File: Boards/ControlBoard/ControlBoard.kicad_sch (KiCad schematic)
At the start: 12 parts, among them J1 TBP02R2W-381-06BE, J11 Conn_02x10_Counter_Clockwise, J12 Conn_02x10_Counter_Clockwise, J13 Conn_02x10_Counter_Clockwise, J14 Conn_02x10_Counter_Clockwise, J2 TBP02R2W-381-06BE, J23 776231-1, J3 TBP01R2W-508-02BE, J4 TBP01R1-508-04BE, J5 Conn_02x10_Counter_Clockwise, J7 TBP02R2W-381-08BE, J8 TBP02R2W-381-08BE

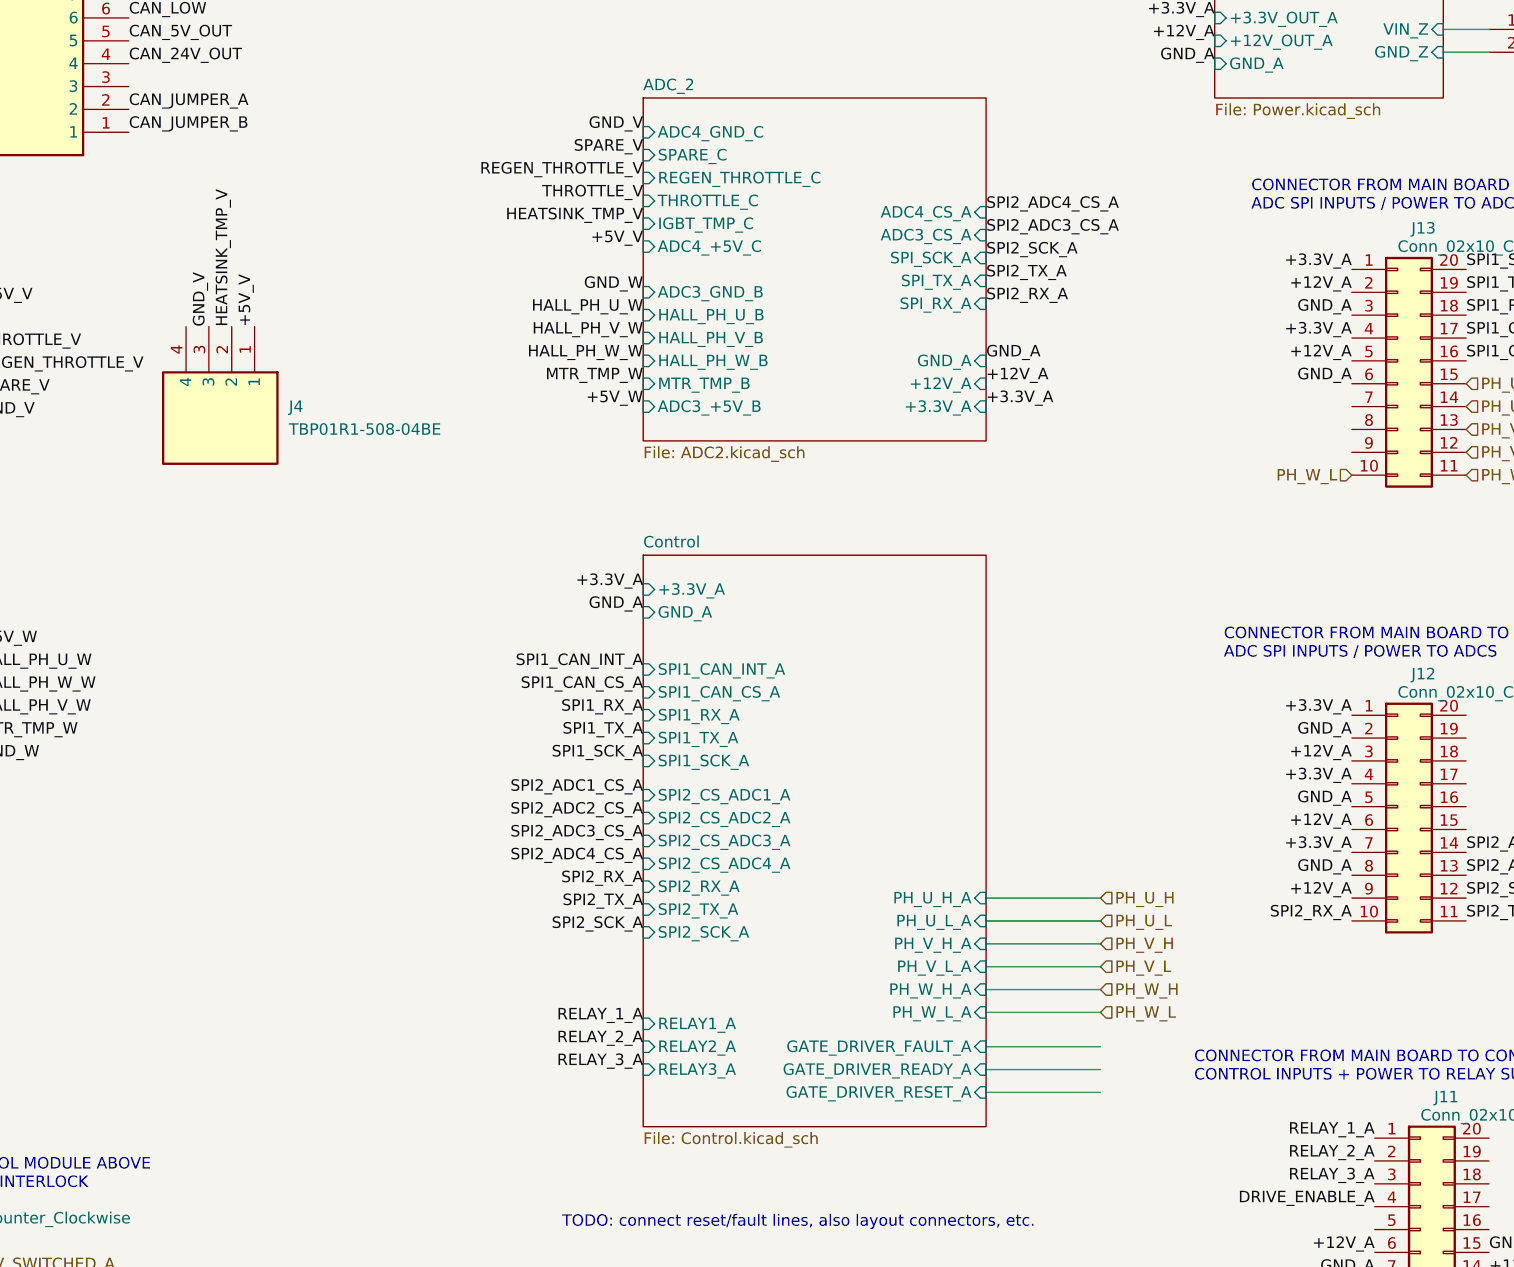
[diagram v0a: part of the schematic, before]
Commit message: layout control boards, add baseplate, refine mechanical layout
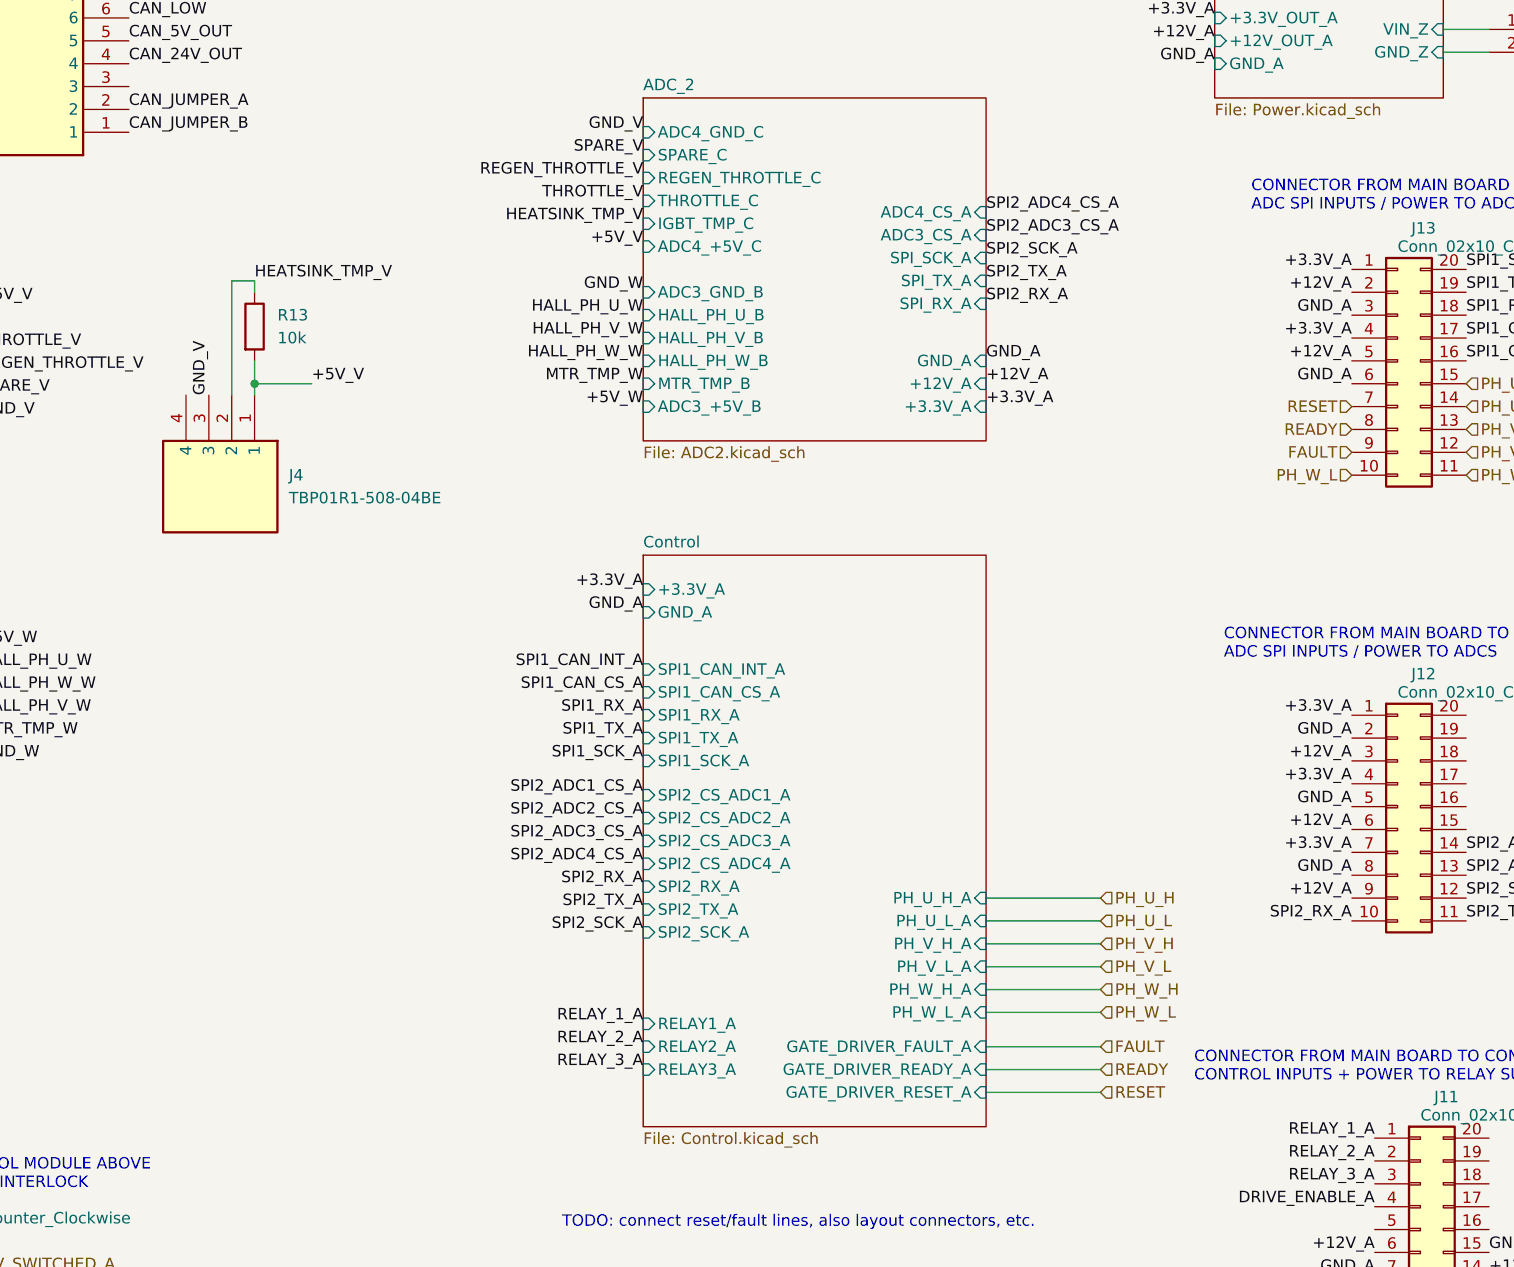
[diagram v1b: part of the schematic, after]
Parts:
- added R13: 10k, Resistor_SMD:R_1210_3225Metric_Pad1.30x2.65mm_HandSolder, symbol Device:R
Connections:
- net +5V_V: now also R13.2
- net HEATSINK_TMP_V: now also R13.1
- net RESET: now reaches J13.7 (Pin_7)
- net READY: now reaches J13.8 (Pin_8)
- net FAULT: now reaches J13.9 (Pin_9)
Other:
- moved on the sheet: J4
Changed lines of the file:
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@@
 		)
+	)
+	(junction
+		(at 71.12 69.85)
+		(diameter 0)
+		(color 0 0 0 0)
 	)
 	(wire
@@
 	(wire
 		(pts
-			(xy 152.4 134.62) (xy 165.1 134.62)
+			(xy 71.12 58.42) (xy 68.58 58.42)
 		)
 		(stroke
@@
 	(wire
 		(pts
-			(xy 203.2 33.02) (xy 208.28 33.02)
+			(xy 152.4 134.62) (xy 165.1 134.62)
 		)
 		(stroke
@@
 	(wire
 		(pts
-			(xy 152.4 137.16) (xy 165.1 137.16)
+			(xy 203.2 33.02) (xy 208.28 33.02)
 		)
 		(stroke
@@
 	(wire
 		(pts
-			(xy 152.4 139.7) (xy 165.1 139.7)
+			(xy 152.4 137.16) (xy 165.1 137.16)
 		)
 		(stroke
@@
 	(wire
 		(pts
-			(xy 152.4 146.05) (xy 165.1 146.05)
+			(xy 152.4 139.7) (xy 165.1 139.7)
 		)
 		(stroke
@@
 	(wire
 		(pts
-			(xy 152.4 132.08) (xy 165.1 132.08)
+			(xy 152.4 146.05) (xy 165.1 146.05)
 		)
 		(stroke
@@
 	(wire
 		(pts
-			(xy 203.2 30.48) (xy 208.28 30.48)
+			(xy 152.4 132.08) (xy 165.1 132.08)
 		)
 		(stroke
@@
 	(wire
 		(pts
-			(xy 152.4 127) (xy 165.1 127)
+			(xy 203.2 30.48) (xy 208.28 30.48)
 		)
 		(stroke
@@
 	(wire
 		(pts
-			(xy 152.4 129.54) (xy 165.1 129.54)
+			(xy 68.58 58.42) (xy 68.58 71.12)
 		)
 		(stroke
@@
 	(wire
 		(pts
-			(xy 152.4 143.51) (xy 165.1 143.51)
+			(xy 152.4 127) (xy 165.1 127)
 		)
 		(stroke
@@
 		)
 	)
+	(wire
+		(pts
+			(xy 152.4 129.54) (xy 165.1 129.54)
+		)
+		(stroke
+			(width 0)
+			(type default)
+		)
+	)
+	(wire
+		(pts
+			(xy 71.12 69.85) (xy 77.47 69.85)
+		)
+		(stroke
+			(width 0)
+			(type default)
+		)
+	)
+	(wire
+		(pts
+			(xy 71.12 69.85) (xy 71.12 71.12)
+		)
+		(stroke
+			(width 0)
+			(type default)
+		)
+	)
+	(wire
+		(pts
+			(xy 152.4 143.51) (xy 165.1 143.51)
+		)
+		(stroke
+			(width 0)
+			(type default)
+		)
+	)
+	(wire
+		(pts
+			(xy 71.12 59.69) (xy 71.12 58.42)
+		)
+		(stroke
+			(width 0)
+			(type default)
+		)
+	)
+	(wire
+		(pts
+			(xy 71.12 67.31) (xy 71.12 69.85)
+		)
+		(stroke
+			(width 0)
+			(type default)
+		)
+	)
 	(label "RELAY1_COM"
 		(at 36.83 185.42 0)
@@
 	)
 	(label "+5V_V"
-		(at 71.12 63.5 90)
+		(at 77.47 69.85 0)
 		(effects
 			(font
@@
 	)
 	(label "GND_V"
-		(at 66.04 63.5 90)
+		(at 66.04 71.12 90)
 		(effects
 			(font
@@
 	)
 	(label "HEATSINK_TMP_V"
-		(at 68.58 63.5 90)
+		(at 71.12 58.42 0)
 		(effects
 			(font
@@
 			)
 			(justify right bottom)
+		)
+	)
+	(hierarchical_label "RESET"
+		(shape input)
+		(at 193.04 72.39 180)
+		(effects
+			(font
+				(size 1.27 1.27)
+			)
+			(justify right)
 		)
 	)
@@
 		)
 	)
+	(hierarchical_label "FAULT"
+		(shape input)
+		(at 193.04 77.47 180)
+		(effects
+			(font
+				(size 1.27 1.27)
+			)
+			(justify right)
+		)
+	)
 	(hierarchical_label "+12V_SWITCHED_A"
 		(shape input)
@@
 		)
 	)
+	(hierarchical_label "RESET"
+		(shape input)
+		(at 165.1 148.59 0)
+		(effects
+			(font
+				(size 1.27 1.27)
+			)
+			(justify left)
+		)
+	)
+	(hierarchical_label "FAULT"
+		(shape input)
+		(at 165.1 143.51 0)
+		(effects
+			(font
+				(size 1.27 1.27)
+			)
+			(justify left)
+		)
+	)
 	(hierarchical_label "PH_V_H"
 		(shape input)
@@
 		(shape input)
 		(at 165.1 127 0)
+		(effects
+			(font
+				(size 1.27 1.27)
+			)
+			(justify left)
+		)
+	)
+	(hierarchical_label "READY"
+		(shape input)
+		(at 193.04 74.93 180)
+		(effects
+			(font
+				(size 1.27 1.27)
+			)
+			(justify right)
+		)
+	)
+	(hierarchical_label "READY"
+		(shape input)
+		(at 165.1 146.05 0)
 		(effects
 			(font
@@
 	)
 	(symbol
+		(lib_id "Device:R")
+		(at 71.12 63.5 0)
+		(unit 1)
+		(exclude_from_sim no)
+		(in_bom yes)
+		(on_board yes)
+		(dnp no)
+		(fields_autoplaced yes)
+		(property "Reference" "R13"
+			(at 73.66 62.2299 0)
+			(effects
+				(font
+					(size 1.27 1.27)
+				)
+				(justify left)
+			)
+		)
+		(property "Value" "10k"
+			(at 73.66 64.7699 0)
+			(effects
+				(font
+					(size 1.27 1.27)
+				)
+				(justify left)
+			)
+		)
+		(property "Footprint" "Resistor_SMD:R_1210_3225Metric_Pad1.30x2.65mm_HandSolder"
+			(at 69.342 63.5 90)
+			(effects
+				(font
+					(size 1.27 1.27)
+				)
+				(hide yes)
+			)
+		)
+		(property "Datasheet" "~"
+			(at 71.12 63.5 0)
+			(effects
+				(font
+					(size 1.27 1.27)
+				)
+				(hide yes)
+			)
+		)
+		(property "Description" "Resistor"
+			(at 71.12 63.5 0)
+			(effects
+				(font
+					(size 1.27 1.27)
+				)
+				(hide yes)
+			)
+		)
+		(pin "1"
+		)
+		(pin "2"
+		)
+		(instances
+			(project "ControlBoard"
+				(path "/66e49eb5-2741-49e2-b48a-baf482488ca8"
+					(reference "R13")
+					(unit 1)
+				)
+			)
+		)
+	)
+	(symbol
 		(lib_id "InverterCom:TBP01R2W-508-02BE")
 		(at 208.28 30.48 0)
@@
 	(symbol
 		(lib_id "InverterCom:TBP01R1-508-04BE")
-		(at 71.12 63.5 270)
+		(at 71.12 71.12 270)
 		(unit 1)
 		(exclude_from_sim no)
@@
 		(fields_autoplaced yes)
 		(property "Reference" "J4"
-			(at 74.93 72.3899 90)
+			(at 74.93 80.0099 90)
 			(effects
 				(font
@@
 		)
 		(property "Value" "TBP01R1-508-04BE"
-			(at 74.93 74.9299 90)
+			(at 74.93 82.5499 90)
 			(effects
 				(font
@@
 		)
 		(property "Footprint" "TBP01R150804BE"
-			(at -23.8 80.01 0)
+			(at -23.8 87.63 0)
 			(effects
 				(font
@@
 		)
 		(property "Datasheet" "https://www.sameskydevices.com/product/resource/supplyframepdf/tbp01r1-508.pdf"
-			(at -123.8 80.01 0)
+			(at -123.8 87.63 0)
 			(effects
 				(font
@@
 		)
 		(property "Description" "2~24 Poles, Pluggable, Receptacle, Horizontal, 5.08 Pitch, Terminal Block Connector"
-			(at 71.12 63.5 0)
+			(at 71.12 71.12 0)
 			(effects
 				(font
@@
 		)
 		(property "Height" "8.9"
-			(at -323.8 80.01 0)
+			(at -323.8 87.63 0)
 			(effects
 				(font
@@
 		)
 		(property "Mouser Part Number" "490-TBP01R1-508-04BE"
-			(at -423.8 80.01 0)
+			(at -423.8 87.63 0)
 			(effects
 				(font
@@
 		)
 		(property "Mouser Price/Stock" "https://www.mouser.co.uk/ProductDetail/Same-Sky/TBP01R1-508-04BE?qs=PzGy0jfpSMtbuigPwCNi2Q%3D%3D"
-			(at -523.8 80.01 0)
+			(at -523.8 87.63 0)
 			(effects
 				(font
@@
 		)
 		(property "Manufacturer_Name" "Same Sky"
-			(at -623.8 80.01 0)
+			(at -623.8 87.63 0)
 			(effects
 				(font
@@
 		)
 		(property "Manufacturer_Part_Number" "TBP01R1-508-04BE"
-			(at -723.8 80.01 0)
-			(effects
-				(font
+			(at -723.8 87.63 0)
+			(effects
+				(font

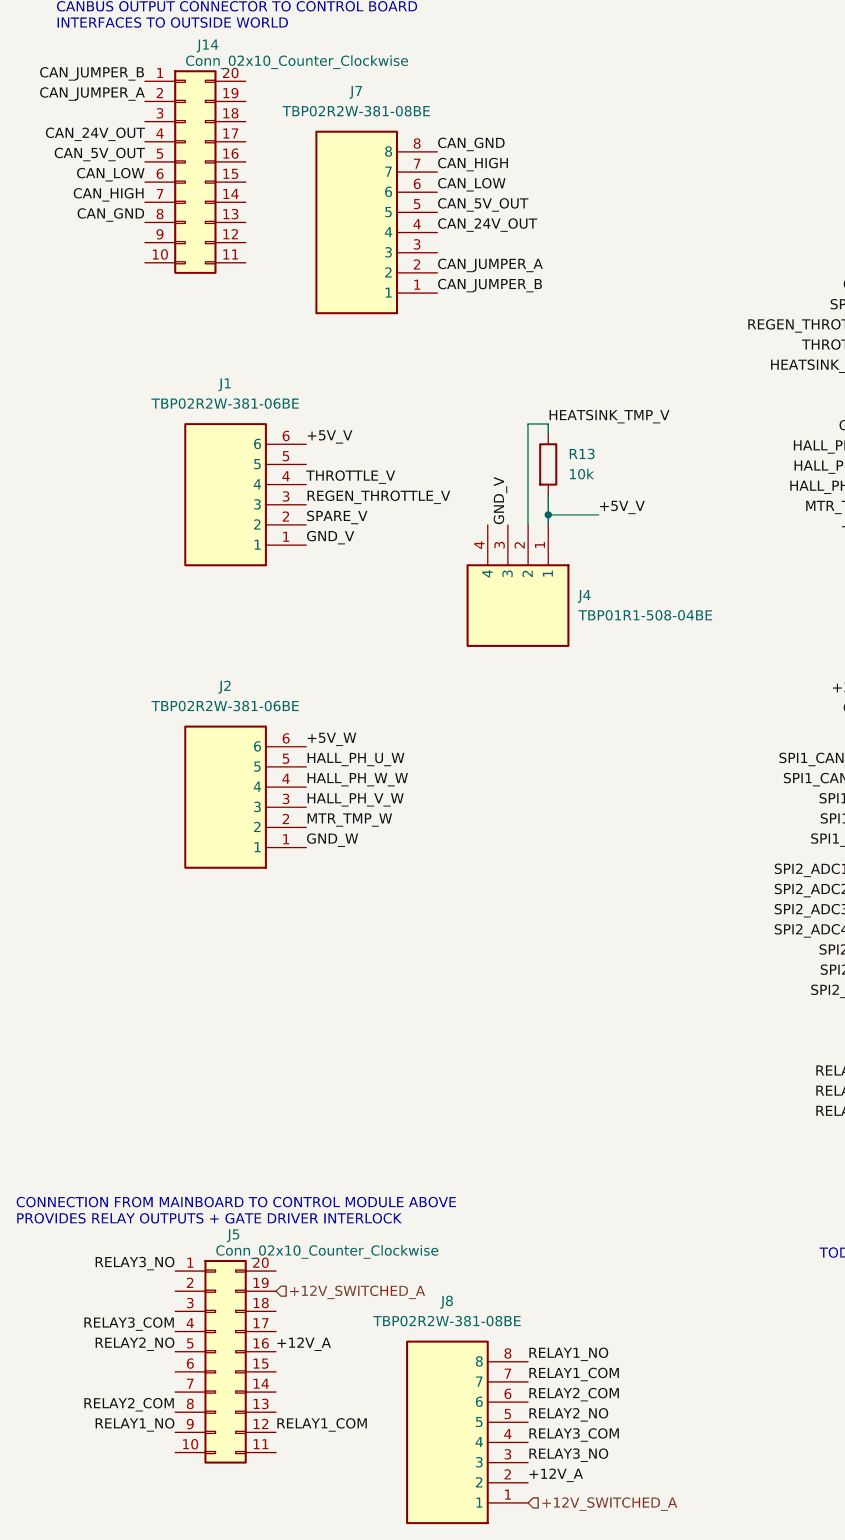
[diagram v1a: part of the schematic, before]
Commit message: Layout mainboard, add EMI filter caps
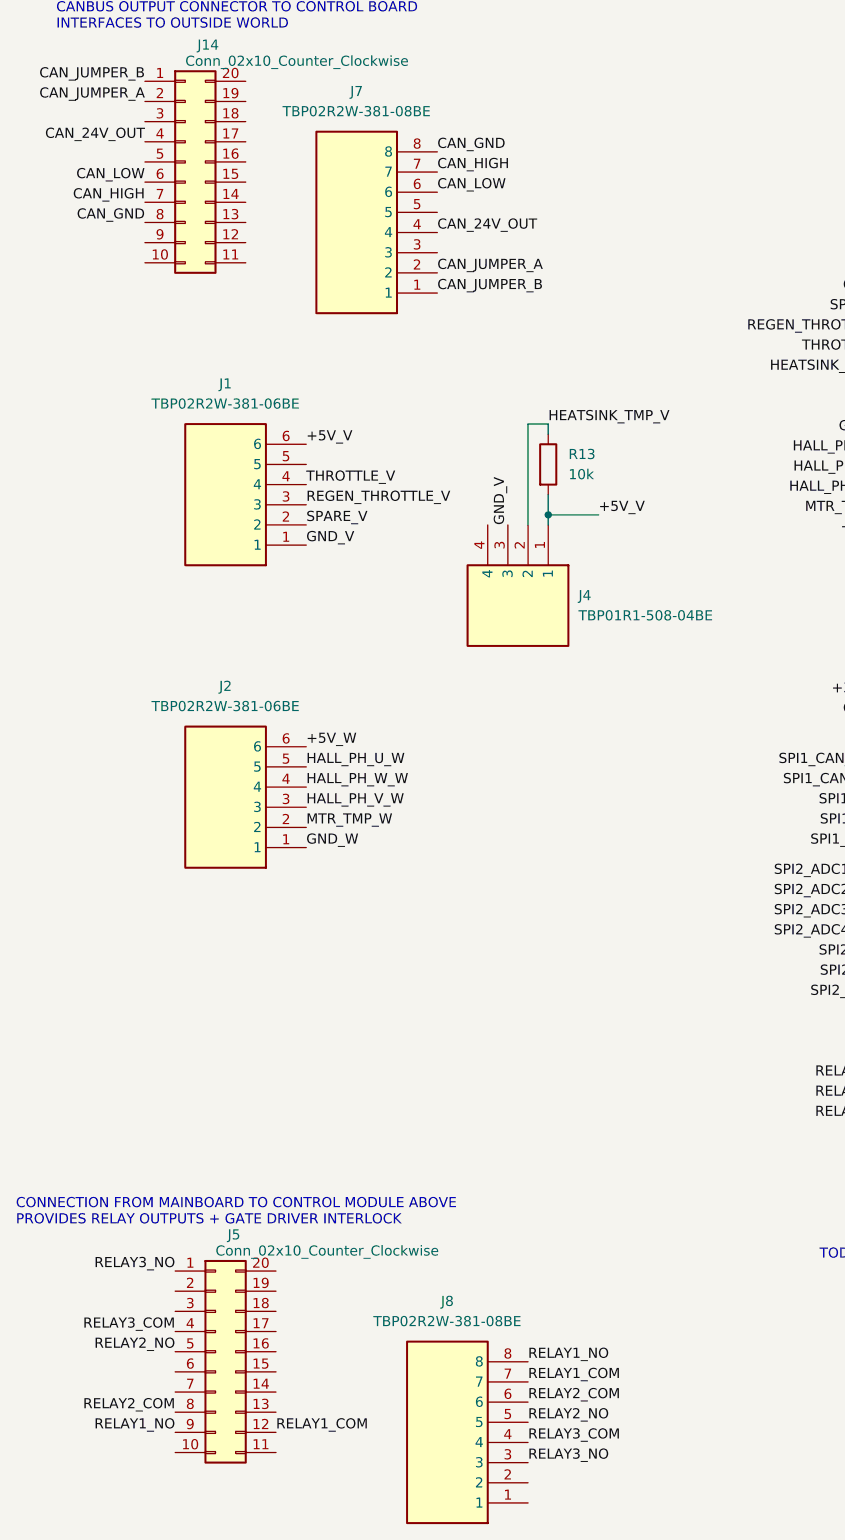
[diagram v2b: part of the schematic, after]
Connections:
- net +12V_A: no longer J5.16 (Pin_16), J8.2
- net +12V_SWITCHED_A: no longer names the net of J8.1
- net +12V_SWITCHED_A: no longer J5.19 (Pin_19)
- net CAN_5V_OUT: no longer names the net of J14.5 (Pin_5)
- net CAN_5V_OUT: no longer J7.5
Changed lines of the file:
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@@
-		)
-	)
-	(label "CAN_5V_OUT"
-		(at 57.15 31.75 0)
-		(effects
-			(font
-				(size 1.27 1.27)
-			)
-			(justify left bottom)
 		)
 	)
@@
 		)
 	)
-	(label "+12V_A"
-		(at 36.83 175.26 0)
-		(effects
-			(font
-				(size 1.27 1.27)
-			)
-			(justify left bottom)
-		)
-	)
-	(label "CAN_5V_OUT"
-		(at 20.32 25.4 180)
-		(effects
-			(font
-				(size 1.27 1.27)
-			)
-			(justify right bottom)
-		)
-	)
 	(label "GND_V"
 		(at 40.64 73.66 0)
@@
 			)
 			(justify right bottom)
-		)
-	)
-	(label "+12V_A"
-		(at 68.58 191.77 0)
-		(effects
-			(font
-				(size 1.27 1.27)
-			)
-			(justify left bottom)
 		)
 	)
@@
 		)
 	)
-	(hierarchical_label "+12V_SWITCHED_A"
-		(shape input)
-		(at 36.83 167.64 0)
-		(effects
-			(font
-				(size 1.27 1.27)
-			)
-			(justify left)
-		)
-	)
 	(hierarchical_label "PH_W_L"
 		(shape input)
@@
 		(effects
 			(font
-				(size 1.27 1.27)
-			)
-			(justify left)
-		)
-	)
-	(hierarchical_label "+12V_SWITCHED_A"
-		(shape input)
-		(at 68.58 194.31 0)
-		(effects
-			(font
